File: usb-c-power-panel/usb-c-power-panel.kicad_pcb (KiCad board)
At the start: 2 copper layers, 25 x 14.1 mm, 24 parts

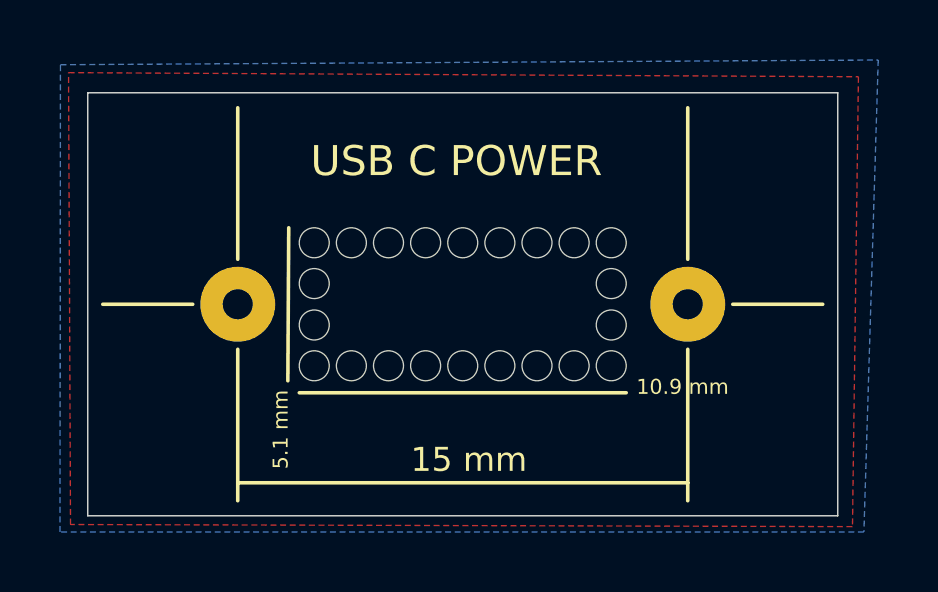
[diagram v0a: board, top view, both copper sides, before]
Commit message: usb c power panel updated measurement pcb
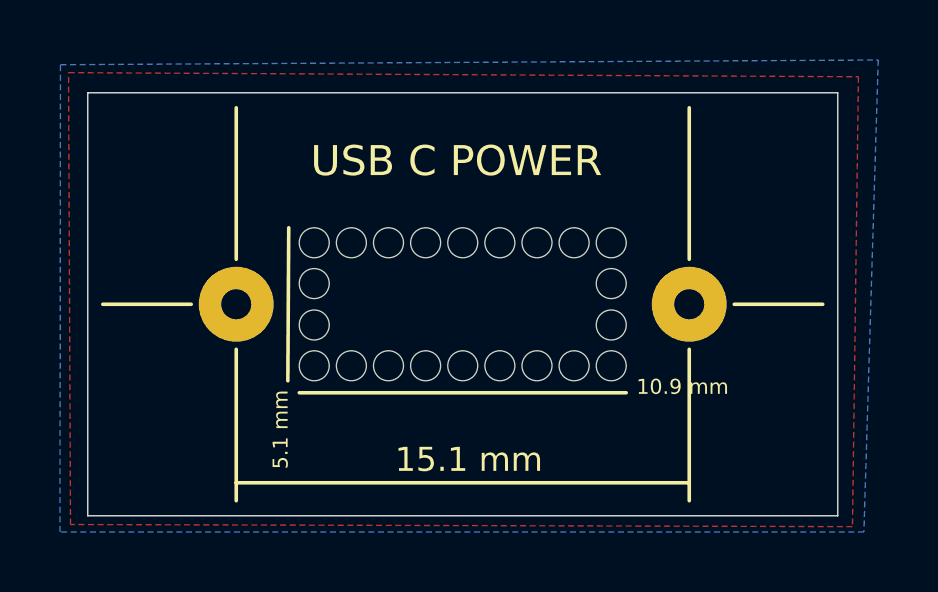
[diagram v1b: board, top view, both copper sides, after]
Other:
- board text added: "15.1 mm"
- board text removed: "15 mm"
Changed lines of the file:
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@@
   )
   (module Connector_Wire:SolderWirePad_1x01_Drill1mm (layer F.Cu)
-    (at 120 107.05)
+    (at 120.05 107.05)
     (descr "Wire solder connection")
     (tags connector)
@@
   )
   (module Connector_Wire:SolderWirePad_1x01_Drill1mm (layer F.Cu)
-    (at 105 107.05)
+    (at 104.95 107.05)
     (descr "Wire solder connection")
     (tags connector)
@@
     (pad "" np_thru_hole circle (at 0 0) (size 1 1) (drill 1) (layers *.Cu *.Mask))
   )
-  (gr_line (start 105 113) (end 120 113) (layer F.SilkS) (width 0.12))
+  (gr_line (start 104.95 113) (end 120.05 113) (layer F.SilkS) (width 0.12))
   (gr_text "10.9 mm" (at 119.82704 109.8042) (layer F.SilkS)
     (effects (font (size 0.5 0.5) (thickness 0.125)))
@@
     (effects (font (size 0.5 0.5) (thickness 0.125)))
   )
-  (gr_text "15 mm" (at 112.70488 112.23244) (layer F.SilkS)
+  (gr_text "15.1 mm" (at 112.70488 112.23244) (layer F.SilkS)
     (effects (font (size 0.8 0.8) (thickness 0.15)))
   )
@@
     (effects (font (size 1 1) (thickness 0.15)))
   )
-  (gr_line (start 120 108.55) (end 120 113.6) (layer F.SilkS) (width 0.12))
-  (gr_line (start 120 100.5) (end 120 105.55) (layer F.SilkS) (width 0.12))
-  (gr_line (start 105 108.55) (end 105 113.6) (layer F.SilkS) (width 0.12))
-  (gr_line (start 105 100.5) (end 105 105.55) (layer F.SilkS) (width 0.12))
-  (gr_line (start 121.5 107.05) (end 124.5 107.05) (layer F.SilkS) (width 0.12))
-  (gr_line (start 100.5 107.05) (end 103.5 107.05) (layer F.SilkS) (width 0.12))
+  (gr_line (start 120.05 108.55) (end 120.05 113.6) (layer F.SilkS) (width 0.12))
+  (gr_line (start 120.05 100.5) (end 120.05 105.55) (layer F.SilkS) (width 0.12))
+  (gr_line (start 104.95 108.55) (end 104.95 113.6) (layer F.SilkS) (width 0.12))
+  (gr_line (start 104.95 100.5) (end 104.95 105.55) (layer F.SilkS) (width 0.12))
+  (gr_line (start 121.55 107.05) (end 124.5 107.05) (layer F.SilkS) (width 0.12))
+  (gr_line (start 100.5 107.05) (end 103.45 107.05) (layer F.SilkS) (width 0.12))
   (gr_line (start 125 100) (end 125 114.1) (layer Edge.Cuts) (width 0.05))
   (gr_line (start 100 100) (end 100 114.1) (layer Edge.Cuts) (width 0.05))
